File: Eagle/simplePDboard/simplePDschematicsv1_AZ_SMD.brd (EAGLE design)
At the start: 51.7 x 38.1 mm, 14 parts, among them IC1 OP27Z

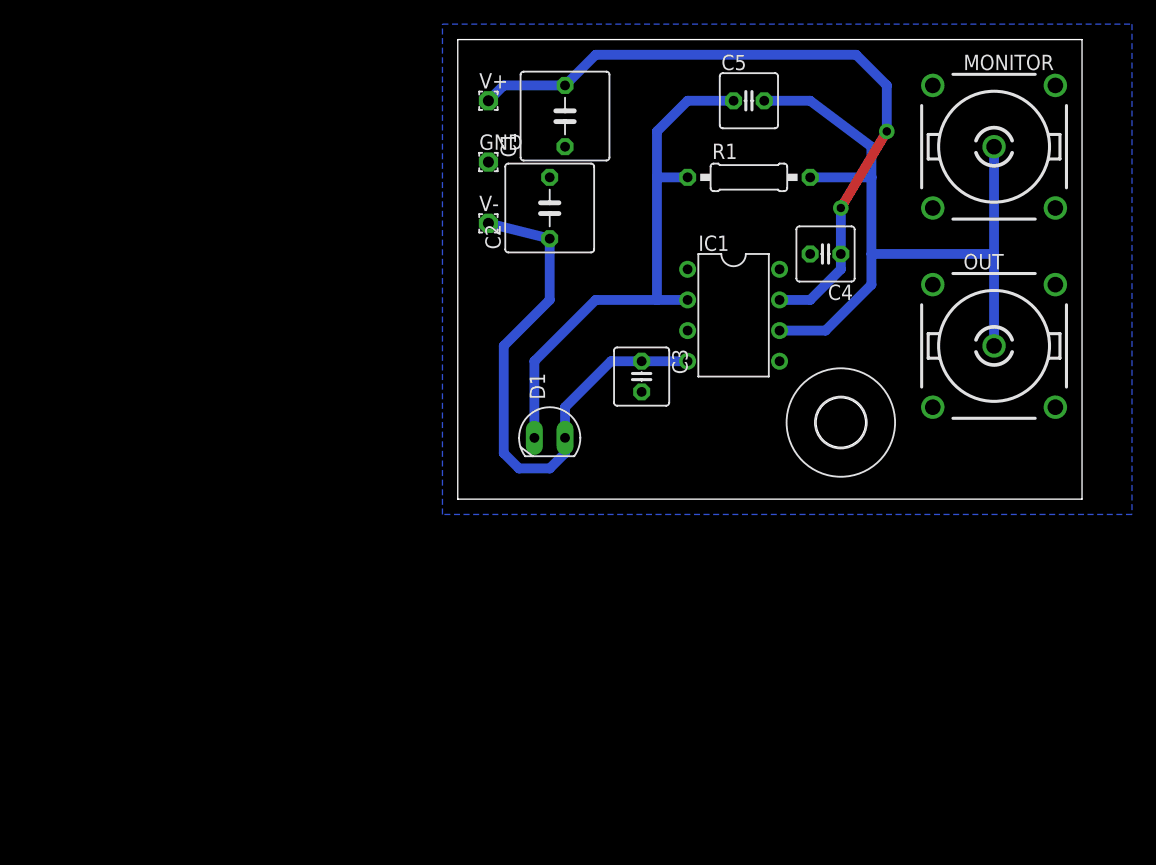
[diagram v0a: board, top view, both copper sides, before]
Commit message: A very simple Transimpedence design. The version we finally test is the version AZ_SMD
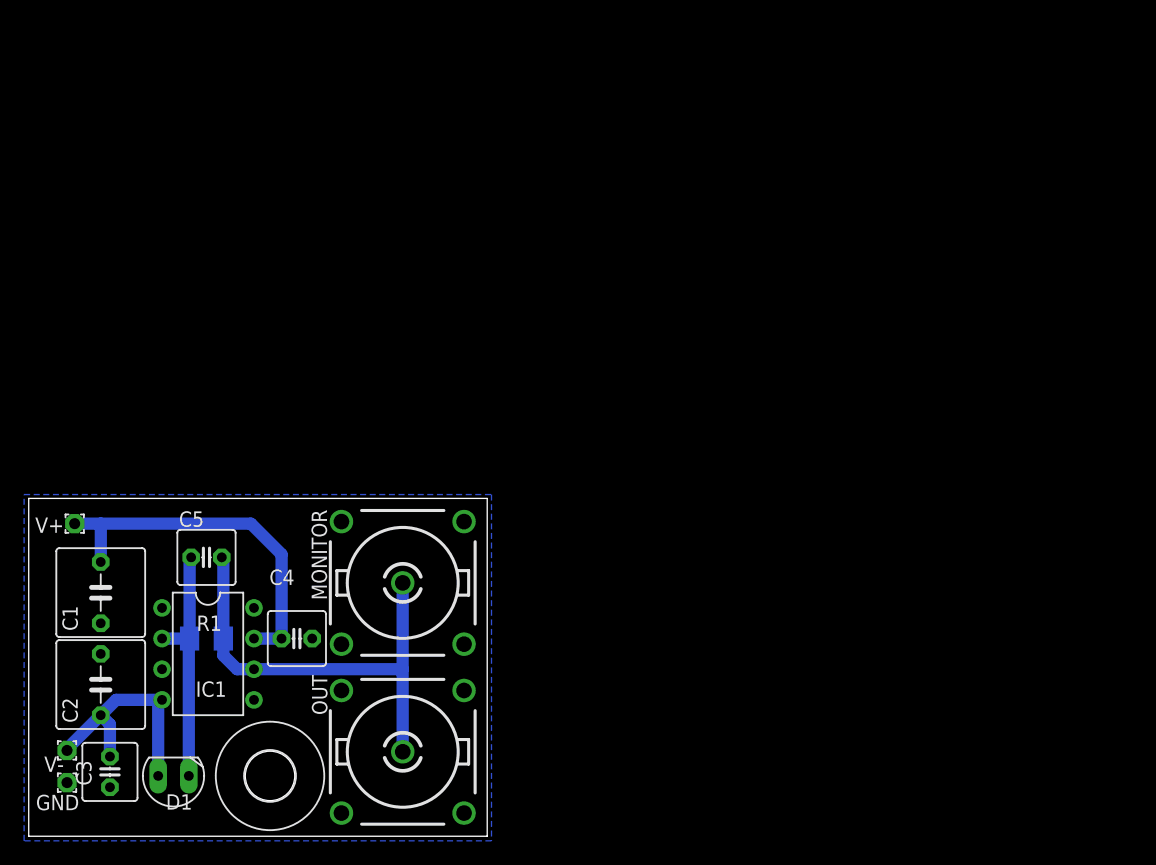
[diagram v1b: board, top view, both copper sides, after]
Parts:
- H1: value MOUNT-HOLE4.1 -> 4.1
- R1: device resistor:0207/10 -> resistor:M1206
- moved GND 62.2 mm to (3.17, 4.45), turned to 180 degrees
- moved MONITOR 60.9 mm to (31.0, 21.0)
- moved OUT 59.4 mm to (31.0, 7.00)
- moved R1 59.0 mm to (14.7, 16.4), flipped to the bottom, turned to 180 degrees
- moved C5 58.8 mm to (14.7, 23.1)
- moved V- 55.9 mm to (3.17, 7.11), turned to 180 degrees
- moved H1 55.6 mm to (20.0, 5.00)
- moved C1 55.1 mm to (5.97, 20.2)
- moved C3 54.9 mm to (6.73, 5.33)
- moved C2 54.3 mm to (5.97, 12.6)
- moved C4 54.2 mm to (22.2, 16.4), turned to 0 degrees
- moved IC1 51.8 mm to (14.9, 15.1)
- moved V+ 49.0 mm to (3.81, 25.9), turned to 180 degrees
- moved D1 41.9 mm to (12.0, 5.00), turned to 270 degrees
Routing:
- net V+: track 58.1 -> 30.6 mm, vias 2 -> 0
- net V-: track 46.3 -> 20.1 mm
- net N$2: track 62.5 -> 37.5 mm
- net N$1: track 45.1 -> 20.5 mm
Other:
- board size 51.7 x 38.1 mm -> 38 x 28 mm
